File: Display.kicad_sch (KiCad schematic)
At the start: 3 parts, among them U4 X1000, U8 M25PX32-VMW, U9 TFP410PAP

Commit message: Update (Display)
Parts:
- added R50, R51, R52, R53: R, symbol Device:R
- added unit 5 of U4
- U4: footprint (none) -> TheBrutzlers_Lib:BGA256C80P16X16_1300X1300X130N
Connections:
- net +3V3: now also R51.2, R52.2, R53.2
- net GND: now also R50.2
- net E-PAPER/XD14: now reaches U4.A11 (SD14_SLCD_D14_CIM_D5_PA14)
- net E-PAPER/XD10: now reaches U4.A15 (SD10_SLCD_D10_CIM_VSYN_PA10)
- net E-PAPER/XD15: now reaches U4.B11 (SD15_SLCD_D15_CIM_D4_PA15)
- net E-PAPER/XD9: now reaches U4.B15 (SD9_SLCD_D9_CIM_HSYN_PA09)
- net E-PAPER/XD7: now reaches U4.B16 (SD7_SLCD_D7_PA07)
- net E-PAPER/XD13: now reaches U4.C11 (SD13_SLCD_D13_CIM_D6_PA13)
- net E-PAPER/XD11: now reaches U4.C14 (SD11_SLCD_D11_CIM_MCLK_PA11)
- net E-PAPER/XD8: now reaches U4.C15 (SD8_SLCD_D8_CIM_PCLK_PA08)
- net E-PAPER/XD5: now reaches U4.C16 (SD5_SLCD_D5_UART1_TXD_PA05)
- net E-PAPER/XD12: now reaches U4.D11 (SD12_SLCD_D12_CIM_D7_PA12)
- net E-PAPER/XD4: now reaches U4.D16 (SD4_SLCD_D4_UART1_RXD_PA04)
- net E-PAPER/XD6: now reaches U4.E15 (SD6_SLCD_D6_PA06)
- net E-PAPER/XD2: now reaches U4.E16 (SD2_SLCD_D2_UART2_RXD_PA02)
- net E-PAPER/XD3: now reaches U4.F15 (SD3_SLCD_D3_UART2_TXD_PA03)
- net E-PAPER/XD0: now reaches U4.F16 (SD0_SLCD_D0_I2C1_SCK_PA00)
- net E-PAPER/XD1: now reaches U4.G15 (SD1_SLCD_D1_I2C1_SDA_PA01)
- new net E-PAPER/XCLK: U4.P3 (SSI0_CLK_I2C2_SCK_PD00)
- new net E-PAPER/XMODE: R50.1, R51.1
- new net E-PAPER/XPWR_GOOD: U4.G3 (DMIC0_IN_PB22)
- new net E-PAPER/XSCL: R53.1, U4.J2 (I2C0_SCK_SCC_CLK_PB23)
- new net E-PAPER/XSDA: R52.1, U4.H1 (I2C0_SDA_SCC_DATA_PB24)
- new net E-PAPER/X~{INT}: U4.R5 (DMIC_CLK_PB21)
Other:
- sheet E-PAPER ports: added XBORDER, XCKV, XCLK, XD0, XD1, XD10, XD11, XD12, XD13, XD14, XD15, XD2, XD3, XD4, XD5, XD6, XD7, XD8, XD9, XLE, XMODE, XOE, XPWRUP, XPWR_GOOD, XSCL, XSDA, XSPV, XSTL, XVCOM_CTRL, XWAKEU, X~{INT}; removed none
- moved on the sheet: U9

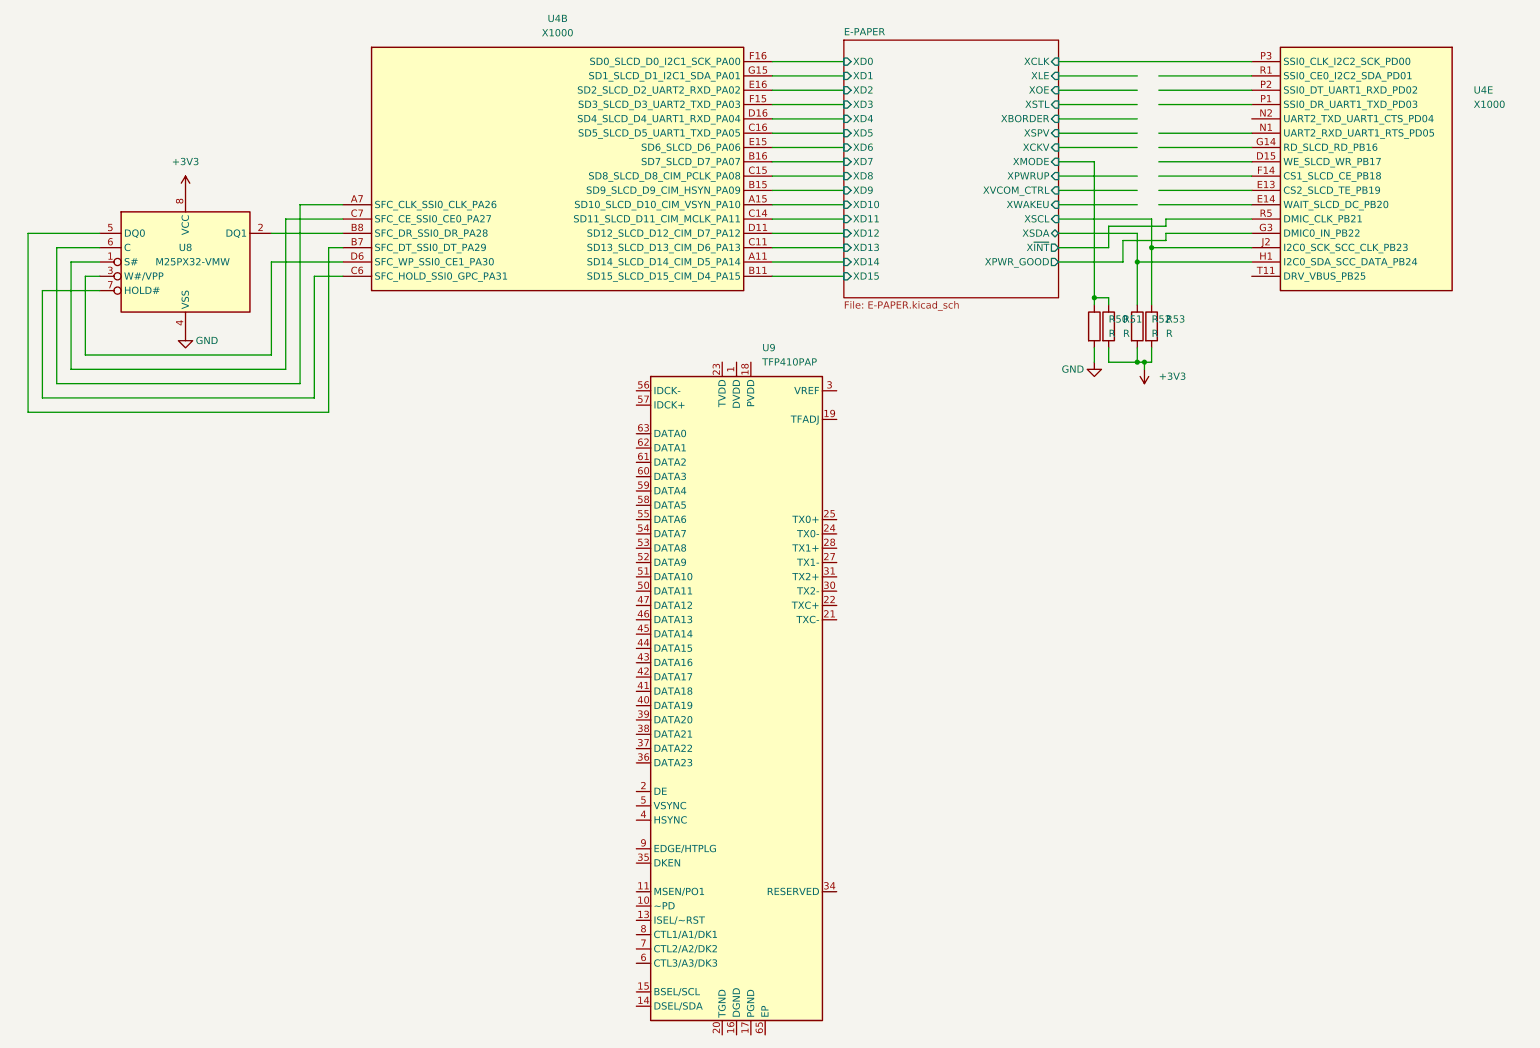
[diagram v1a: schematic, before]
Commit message: Add Audio
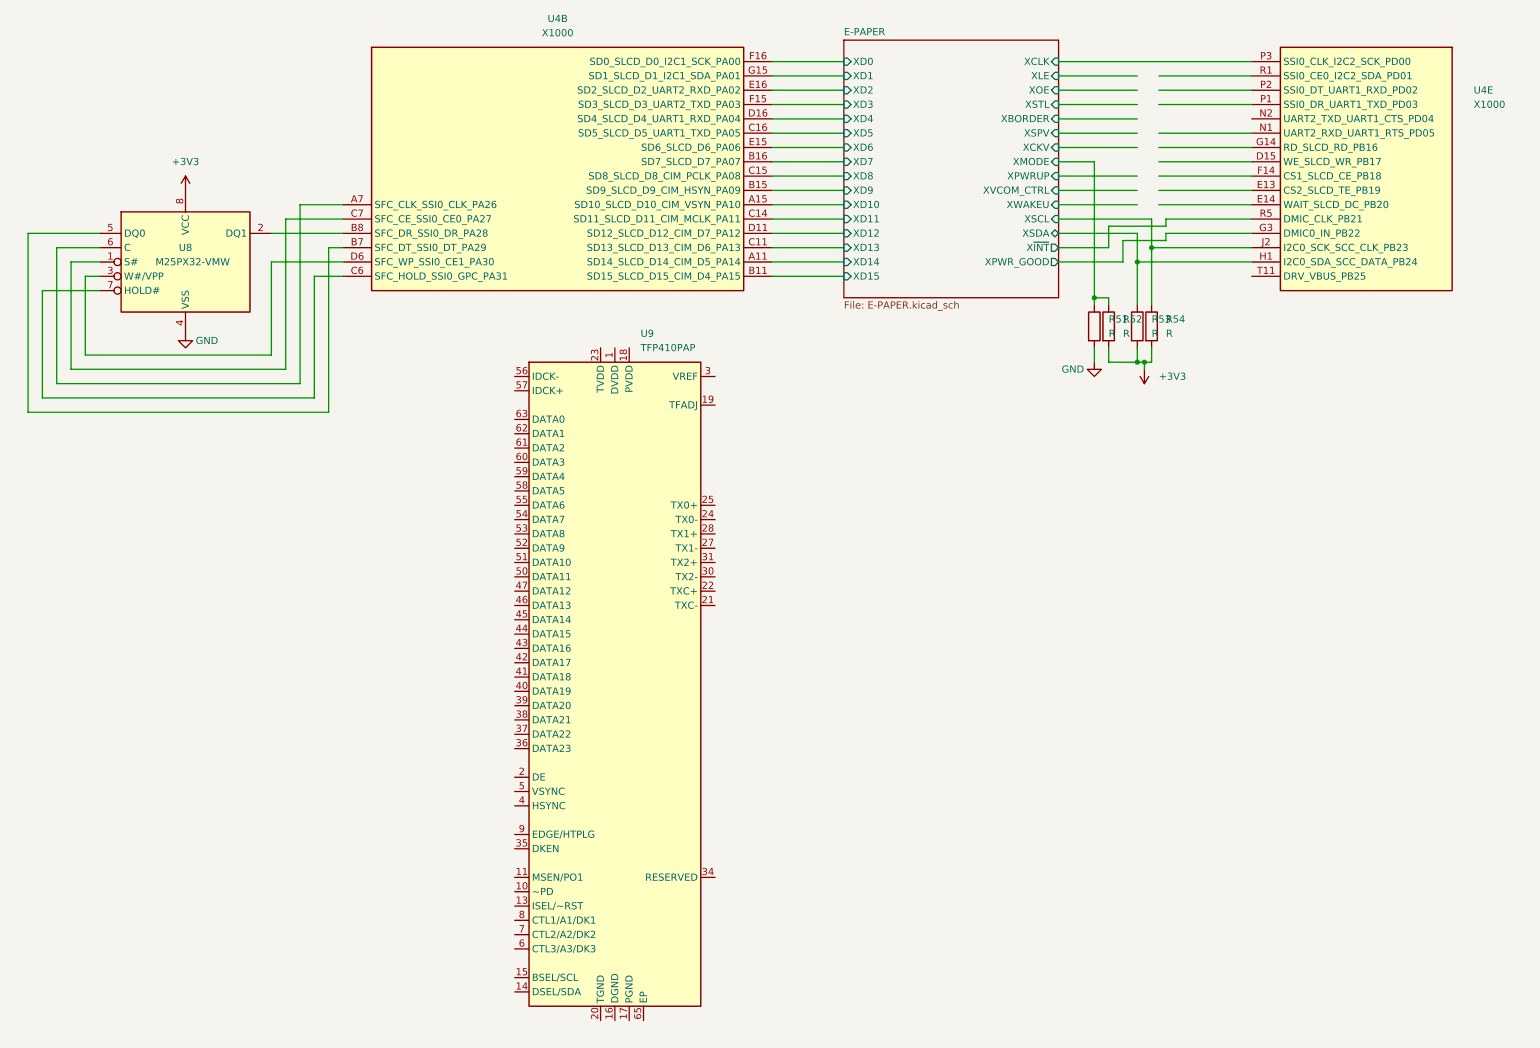
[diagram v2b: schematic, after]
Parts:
- renumbered R50 to R51, R51 to R52, R52 to R53, R53 to R54
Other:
- moved on the sheet: U9
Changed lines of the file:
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@@
   (symbol (lib_id "Device:R") (at 204.47 68.58 0) (unit 1)
     (in_bom yes) (on_board yes) (fields_autoplaced)
-    (property "Reference" "R50" (id 0) (at 207.01 67.3099 0)
+    (property "Reference" "R51" (id 0) (at 207.01 67.3099 0)
       (effects (font (size 1.27 1.27)) (justify left))
     )
@@
   (symbol (lib_id "Device:R") (at 207.01 68.58 0) (unit 1)
     (in_bom yes) (on_board yes) (fields_autoplaced)
-    (property "Reference" "R51" (id 0) (at 209.55 67.3099 0)
+    (property "Reference" "R52" (id 0) (at 209.55 67.3099 0)
       (effects (font (size 1.27 1.27)) (justify left))
     )
@@
   (symbol (lib_id "Device:R") (at 214.63 68.58 0) (unit 1)
     (in_bom yes) (on_board yes) (fields_autoplaced)
-    (property "Reference" "R53" (id 0) (at 217.17 67.3099 0)
+    (property "Reference" "R54" (id 0) (at 217.17 67.3099 0)
       (effects (font (size 1.27 1.27)) (justify left))
     )
@@
   (symbol (lib_id "power:+3V3") (at 213.36 76.2 180) (unit 1)
     (in_bom yes) (on_board yes) (fields_autoplaced)
-    (property "Reference" "#PWR096" (id 0) (at 213.36 72.39 0)
+    (property "Reference" "#PWR099" (id 0) (at 213.36 72.39 0)
       (effects (font (size 1.27 1.27)) hide)
     )
@@
   (symbol (lib_id "power:+3V3") (at 43.18 44.45 0) (unit 1)
     (in_bom yes) (on_board yes) (fields_autoplaced)
-    (property "Reference" "#PWR093" (id 0) (at 43.18 48.26 0)
+    (property "Reference" "#PWR096" (id 0) (at 43.18 48.26 0)
       (effects (font (size 1.27 1.27)) hide)
     )
@@
   (symbol (lib_id "power:GND") (at 43.18 69.85 0) (unit 1)
     (in_bom yes) (on_board yes)
-    (property "Reference" "#PWR094" (id 0) (at 43.18 76.2 0)
+    (property "Reference" "#PWR097" (id 0) (at 43.18 76.2 0)
       (effects (font (size 1.27 1.27)) hide)
     )
@@
   (symbol (lib_id "power:GND") (at 204.47 74.93 0) (unit 1)
     (in_bom yes) (on_board yes)
-    (property "Reference" "#PWR095" (id 0) (at 204.47 81.28 0)
+    (property "Reference" "#PWR098" (id 0) (at 204.47 81.28 0)
       (effects (font (size 1.27 1.27)) hide)
     )
@@
     (pin "1")
   )
-  (symbol (lib_id "Video:TFP410PAP") (at 140.97 133.35 0) (unit 1)
-    (in_bom yes) (on_board yes) (fields_autoplaced)
-    (property "Reference" "U9" (id 0) (at 145.5294 72.39 0)
-      (effects (font (size 1.27 1.27)) (justify left))
-    )
-    (property "Value" "TFP410PAP" (id 1) (at 145.5294 74.93 0)
-      (effects (font (size 1.27 1.27)) (justify left))
-    )
-    (property "Footprint" "Package_QFP:HTQFP-64-1EP_10x10mm_P0.5mm_EP8x8mm_Mask4.4x4.4mm_ThermalVias" (id 2) (at 142.24 194.31 0)
-      (effects (font (size 1.27 1.27)) hide)
-    )
-    (property "Datasheet" "http://www.ti.com/lit/ds/symlink/tfp410.pdf" (id 3) (at 142.24 193.04 0)
+  (symbol (lib_id "Video:TFP410PAP") (at 119.38 130.81 0) (unit 1)
+    (in_bom yes) (on_board yes) (fields_autoplaced)
+    (property "Reference" "U9" (id 0) (at 123.9394 69.85 0)
+      (effects (font (size 1.27 1.27)) (justify left))
+    )
+    (property "Value" "TFP410PAP" (id 1) (at 123.9394 72.39 0)
+      (effects (font (size 1.27 1.27)) (justify left))
+    )
+    (property "Footprint" "Package_QFP:HTQFP-64-1EP_10x10mm_P0.5mm_EP8x8mm_Mask4.4x4.4mm_ThermalVias" (id 2) (at 120.65 191.77 0)
+      (effects (font (size 1.27 1.27)) hide)
+    )
+    (property "Datasheet" "http://www.ti.com/lit/ds/symlink/tfp410.pdf" (id 3) (at 120.65 190.5 0)
       (effects (font (size 1.27 1.27)) hide)
     )
@@
   (symbol (lib_id "Device:R") (at 212.09 68.58 0) (unit 1)
     (in_bom yes) (on_board yes) (fields_autoplaced)
-    (property "Reference" "R52" (id 0) (at 214.63 67.3099 0)
-      (effects (font (size 1.27 1.27)) (justify left))
-    )
+    (property "Reference" "R53" (id 0) (at 214.63 67.3099 0)
+      (effects (font (size 1.27 1.27)) (justify left))
+    )

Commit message: New i.mx6 Version
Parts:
- removed U8: M25PX32-VMW, Package_SO:SOIC-8W_5.3x5.3mm_P1.27mm, symbol Memory_Flash:M25PX32-VMW
- added U? (x2): IMX6UL, TheBrutzlers_Lib:IMX6UL_BGA289, symbol TheBrutzlers_Lib:IMX6UL
